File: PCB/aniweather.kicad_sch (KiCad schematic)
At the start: 26 parts, among them SW1 SW_DIP_x01, SW2 SW_Push, SW3 SW_Push, U5 TPS63001

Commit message: Final revision
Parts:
- added JP1: Jumper_2_Bridged, Resistor_THT:R_Axial_DIN0207_L6.3mm_D2.5mm_P15.24mm_Horizontal, symbol Jumper:Jumper_2_Bridged
- added R5, R6, R7: 10k, Resistor_THT:R_Axial_DIN0207_L6.3mm_D2.5mm_P10.16mm_Horizontal, symbol Device:R
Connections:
- net +3.3V: now also R5.2, R6.2, R7.2
- net CS_LCD: now also R6.1
- net GND: now also JP1.1 (A), JP1.2 (B)
- net MISO: now also R7.1
- net SD_CS: now also R5.1
- no-connect marks 3 -> 7
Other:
- moved on the sheet: C1, C2, C4, C9, R1, U1

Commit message: PCB revision
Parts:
- removed JP1: Jumper_2_Bridged, Resistor_THT:R_Axial_DIN0207_L6.3mm_D2.5mm_P15.24mm_Horizontal, symbol Jumper:Jumper_2_Bridged
- added JP1: Jumper_2_Open, Jumper:SolderJumper-2_P1.3mm_Open_Pad1.0x1.5mm, symbol Jumper:Jumper_2_Open
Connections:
- net at C6.1, R2.2, SW1.2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: now also JP1.1 (A)
- net at SW1.1, U3.2 (OUT+): now also JP1.2 (B)
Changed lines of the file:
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@@
 		(title "Aniweather")
 		(date "2024-12-05")
-		(rev "v1.5")
+		(rev "v1.6")
 		(company "Cyao")
 		(comment 1 "Anime weather station")
@@
 	)
 	(junction
+		(at 201.93 30.48)
+		(diameter 0)
+		(color 0 0 0 0)
+	)
+	(junction
 		(at 49.53 106.68)
 		(diameter 0)
@@
 	(wire
 		(pts
+			(xy 193.04 30.48) (xy 201.93 30.48)
+		)
+		(stroke
+			(width 0)
+			(type default)
+		)
+	)
+	(wire
+		(pts
 			(xy 201.93 55.88) (xy 201.93 54.61)
 		)
@@
 	(wire
 		(pts
+			(xy 193.04 33.02) (xy 193.04 30.48)
+		)
+		(stroke
+			(width 0)
+			(type default)
+		)
+	)
+	(wire
+		(pts
 			(xy 48.26 58.42) (xy 48.26 60.96)
 		)
@@
 	(wire
 		(pts
+			(xy 193.04 46.99) (xy 201.93 46.99)
+		)
+		(stroke
+			(width 0)
+			(type default)
+		)
+	)
+	(wire
+		(pts
 			(xy 36.83 106.68) (xy 31.75 106.68)
 		)
@@
 	(wire
 		(pts
+			(xy 193.04 43.18) (xy 193.04 46.99)
+		)
+		(stroke
+			(width 0)
+			(type default)
+		)
+	)
+	(wire
+		(pts
 			(xy 219.71 67.31) (xy 219.71 66.04)
 		)
@@
 	)
 	(symbol
+		(lib_id "Jumper:Jumper_2_Open")
+		(at 193.04 38.1 90)
+		(unit 1)
+		(exclude_from_sim yes)
+		(in_bom yes)
+		(on_board yes)
+		(dnp no)
+		(property "Reference" "JP1"
+			(at 173.736 36.322 90)
+			(effects
+				(font
+					(size 1.27 1.27)
+				)
+				(justify right)
+			)
+		)
+		(property "Value" "Jumper_2_Open"
+			(at 173.736 38.862 90)
+			(effects
+				(font
+					(size 1.27 1.27)
+				)
+				(justify right)
+			)
+		)
+		(property "Footprint" "Jumper:SolderJumper-2_P1.3mm_Open_Pad1.0x1.5mm"
+			(at 193.04 38.1 0)
+			(effects
+				(font
+					(size 1.27 1.27)
+				)
+				(hide yes)
+			)
+		)
+		(property "Datasheet" "~"
+			(at 193.04 38.1 0)
+			(effects
+				(font
+					(size 1.27 1.27)
+				)
+				(hide yes)
+			)
+		)
+		(property "Description" "Jumper, 2-pole, open"
+			(at 193.04 38.1 0)
+			(effects
+				(font
+					(size 1.27 1.27)
+				)
+				(hide yes)
+			)
+		)
+		(pin "1"
+		)
+		(pin "2"
+		)
+		(instances
+			(project ""
+				(path "/e7e4d5de-a607-486c-961b-1d24c88fafef"
+					(reference "JP1")
+					(unit 1)
+				)
+			)
+		)
+	)
+	(symbol
 		(lib_id "power:+3.3V")
 		(at 22.86 39.37 90)
@@
 	)
 	(symbol
-		(lib_id "power:GND")
-		(at 66.04 59.69 270)
-		(unit 1)
-		(exclude_from_sim no)
-		(in_bom yes)
-		(on_board yes)
-		(dnp no)
-		(fields_autoplaced yes)
-		(property "Reference" "#PWR023"
-			(at 59.69 59.69 0)
-			(effects
-				(font
-					(size 1.27 1.27)
-				)
-				(hide yes)
-			)
-		)
-		(property "Value" "GND"
-			(at 62.23 59.6899 90)
-			(effects
-				(font
-					(size 1.27 1.27)
-				)
-				(justify right)
-			)
-		)
-		(property "Footprint" ""
-			(at 66.04 59.69 0)
-			(effects
-				(font
-					(size 1.27 1.27)
-				)
-				(hide yes)
-			)
-		)
-		(property "Datasheet" ""
-			(at 66.04 59.69 0)
-			(effects
-				(font
-					(size 1.27 1.27)
-				)
-				(hide yes)
-			)
-		)
-		(property "Description" "Power symbol creates a global label with name \"GND\" , ground"
-			(at 66.04 59.69 0)
-			(effects
-				(font
-					(size 1.27 1.27)
-				)
-				(hide yes)
-			)
-		)
-		(pin "1"
-		)
-		(instances
-			(project "aniweather"
-				(path "/e7e4d5de-a607-486c-961b-1d24c88fafef"
-					(reference "#PWR023")
-					(unit 1)
-				)
-			)
-		)
-	)
-	(symbol
 		(lib_id "power:PWR_FLAG")
 		(at 31.75 91.44 0)
@@
 	)
 	(symbol
-		(lib_id "Jumper:Jumper_2_Bridged")
-		(at 71.12 59.69 0)
-		(unit 1)
-		(exclude_from_sim yes)
-		(in_bom yes)
-		(on_board yes)
-		(dnp no)
-		(fields_autoplaced yes)
-		(property "Reference" "JP1"
-			(at 71.12 54.61 0)
-			(effects
-				(font
-					(size 1.27 1.27)
-				)
-			)
-		)
-		(property "Value" "Jumper_2_Bridged"
-			(at 71.12 57.15 0)
-			(effects
-				(font
-					(size 1.27 1.27)
-				)
-			)
-		)
-		(property "Footprint" "Resistor_THT:R_Axial_DIN0207_L6.3mm_D2.5mm_P15.24mm_Horizontal"
-			(at 71.12 59.69 0)
-			(effects
-				(font
-					(size 1.27 1.27)
-				)
-				(hide yes)
-			)
-		)
-		(property "Datasheet" "~"
-			(at 71.12 59.69 0)
-			(effects
-				(font
-					(size 1.27 1.27)
-				)
-				(hide yes)
-			)
-		)
-		(property "Description" "Jumper, 2-pole, closed/bridged"
-			(at 71.12 59.69 0)
-			(effects
-				(font
-					(size 1.27 1.27)
-				)
-				(hide yes)
-			)
-		)
-		(pin "1"
-		)
-		(pin "2"
-		)
-		(instances
-			(project ""
-				(path "/e7e4d5de-a607-486c-961b-1d24c88fafef"
-					(reference "JP1")
-					(unit 1)
-				)
-			)
-		)
-	)
-	(symbol
 		(lib_id "power:+3.3V")
 		(at 106.68 36.83 0)
@@
 					(unit 1)
 				)
-			)
-		)
-	)
-	(symbol
-		(lib_id "power:GND")
-		(at 76.2 59.69 90)
-		(unit 1)
-		(exclude_from_sim no)
-		(in_bom yes)
-		(on_board yes)
-		(dnp no)
-		(fields_autoplaced yes)
-		(property "Reference" "#PWR022"
-			(at 82.55 59.69 0)
-			(effects
-				(font
-					(size 1.27 1.27)
-				)
-				(hide yes)
-			)
-		)
-		(property "Value" "GND"
-			(at 80.01 59.6899 90)
-			(effects
-				(font
-					(size 1.27 1.27)
-				)
-				(justify right)
-			)
-		)
-		(property "Footprint" ""
-			(at 76.2 59.69 0)
-			(effects
-				(font
-					(size 1.27 1.27)
-				)
-				(hide yes)
-			)
-		)
-		(property "Datasheet" ""
-			(at 76.2 59.69 0)
-			(effects
-				(font
-					(size 1.27 1.27)
-				)
-				(hide yes)
-			)
-		)
-		(property "Description" "Power symbol creates a global label with name \"GND\" , ground"
-			(at 76.2 59.69 0)
-			(effects
-				(font
-					(size 1.27 1.27)
-				)
-				(hide yes)
-			)
-		)
-		(pin "1"
-		)
-		(instances
-			(project "aniweather"
-				(path "/e7e4d5de-a607-486c-961b-1d24c88fafef"
-					(reference "#PWR022")
-					(unit 1)
-				)

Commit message: I hope this is the final revision
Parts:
- added JP2, JP3, JP4: Jumper_2_Open, Jumper:SolderJumper-2_P1.3mm_Open_Pad1.0x1.5mm, symbol Jumper:Jumper_2_Open
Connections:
- net GND: now also JP3.1 (A)
- net at JP1.2 (B), SW1.1, U3.2 (OUT+): now also JP4.2 (B)
- net at U3.4 (IN+): now also JP2.1 (A)
- net at U3.5 (IN-): now also JP3.2 (B)
- net VBUS: now reaches U2.14 (VBUS)
- net VBUS: now also JP2.2 (B), JP4.1 (A)
- no-connect marks 7 -> 4

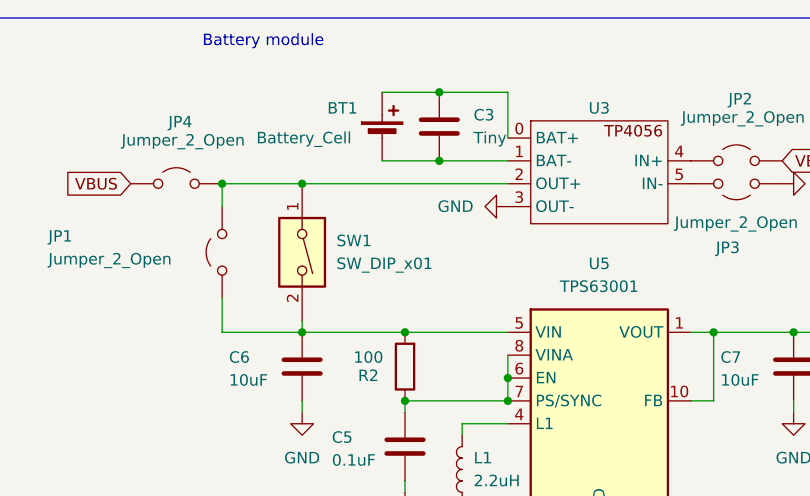
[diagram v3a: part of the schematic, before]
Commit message: Add diode
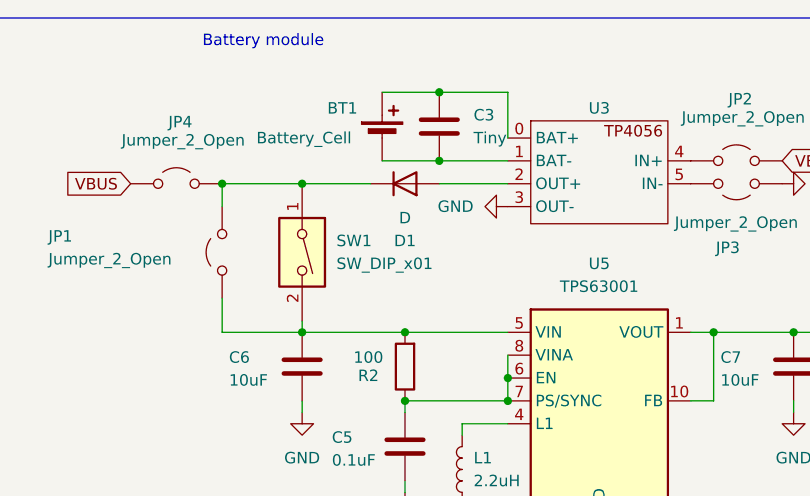
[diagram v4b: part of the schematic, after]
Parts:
- added D1: D, Diode_THT:D_DO-35_SOD27_P7.62mm_Horizontal, symbol Device:D
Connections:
- net at JP1.2 (B), JP4.2 (B), SW1.1: now also D1.1 (K); no longer U3.2 (OUT+)
- new net: D1.2 (A), U3.2 (OUT+)
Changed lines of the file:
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@@
 		(title "Aniweather")
 		(date "2024-12-05")
-		(rev "v1.7")
+		(rev "v1.8")
 		(company "Cyao")
 		(comment 1 "Anime weather station")
@@
 	)
 	(junction
+		(at 49.53 106.68)
+		(diameter 0)
+		(color 0 0 0 0)
+	)
+	(junction
+		(at 48.26 58.42)
+		(diameter 0)
+		(color 0 0 0 0)
+	)
+	(junction
+		(at 106.68 46.99)
+		(diameter 0)
+		(color 0 0 0 0)
+	)
+	(junction
+		(at 49.53 95.25)
+		(diameter 0)
+		(color 0 0 0 0)
+	)
+	(junction
+		(at 256.54 46.99)
+		(diameter 0)
+		(color 0 0 0 0)
+	)
+	(junction
+		(at 267.97 46.99)
+		(diameter 0)
+		(color 0 0 0 0)
+	)
+	(junction
 		(at 201.93 30.48)
-		(diameter 0)
-		(color 0 0 0 0)
-	)
-	(junction
-		(at 49.53 106.68)
-		(diameter 0)
-		(color 0 0 0 0)
-	)
-	(junction
-		(at 48.26 58.42)
-		(diameter 0)
-		(color 0 0 0 0)
-	)
-	(junction
-		(at 106.68 46.99)
-		(diameter 0)
-		(color 0 0 0 0)
-	)
-	(junction
-		(at 49.53 95.25)
-		(diameter 0)
-		(color 0 0 0 0)
-	)
-	(junction
-		(at 256.54 46.99)
-		(diameter 0)
-		(color 0 0 0 0)
-	)
-	(junction
-		(at 267.97 46.99)
 		(diameter 0)
 		(color 0 0 0 0)
@@
 	(wire
 		(pts
-			(xy 201.93 30.48) (xy 224.79 30.48)
-		)
-		(stroke
-			(width 0)
-			(type default)
-		)
-	)
-	(wire
-		(pts
 			(xy 49.53 91.44) (xy 49.53 95.25)
 		)
@@
 	(wire
 		(pts
+			(xy 217.17 30.48) (xy 224.79 30.48)
+		)
+		(stroke
+			(width 0)
+			(type default)
+		)
+	)
+	(wire
+		(pts
 			(xy 269.24 46.99) (xy 267.97 46.99)
 		)
@@
 		(pts
 			(xy 213.36 46.99) (xy 224.79 46.99)
+		)
+		(stroke
+			(width 0)
+			(type default)
+		)
+	)
+	(wire
+		(pts
+			(xy 201.93 30.48) (xy 209.55 30.48)
 		)
 		(stroke
@@
 					(unit 1)
 				)
+			)
+		)
+	)
+	(symbol
+		(lib_id "Device:D")
+		(at 213.36 30.48 0)
+		(mirror x)
+		(unit 1)
+		(exclude_from_sim no)
+		(in_bom yes)
+		(on_board yes)
+		(dnp no)
+		(property "Reference" "D1"
+			(at 213.36 36.83 0)
+			(effects
+				(font
+					(size 1.27 1.27)
+				)
+			)
+		)
+		(property "Value" "D"
+			(at 213.36 34.29 0)
+			(effects
+				(font
+					(size 1.27 1.27)
+				)
+			)
+		)
+		(property "Footprint" "Diode_THT:D_DO-35_SOD27_P7.62mm_Horizontal"
+			(at 213.36 30.48 0)
+			(effects
+				(font
+					(size 1.27 1.27)
+				)
+				(hide yes)
+			)
+		)
+		(property "Datasheet" "~"
+			(at 213.36 30.48 0)
+			(effects
+				(font
+					(size 1.27 1.27)
+				)
+				(hide yes)
+			)
+		)
+		(property "Description" "Diode"
+			(at 213.36 30.48 0)
+			(effects
+				(font
+					(size 1.27 1.27)
+				)
+				(hide yes)
+			)
+		)
+		(property "Sim.Device" "D"
+			(at 213.36 30.48 0)
+			(effects
+				(font
+					(size 1.27 1.27)
+				)
+				(hide yes)
+			)
+		)
+		(property "Sim.Pins" "1=K 2=A"
+			(at 213.36 30.48 0)
+			(effects
+				(font
+					(size 1.27 1.27)
+				)
+				(hide yes)
+			)
+		)
+		(pin "1"
+		)
+		(pin "2"
+		)
+		(instances
+			(project ""
+				(path "/e7e4d5de-a607-486c-961b-1d24c88fafef"
+					(reference "D1")
+					(unit 1)
+				)

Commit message: Hope last rev
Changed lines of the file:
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@@
 	(rectangle
 		(start 165.1 12.065)
-		(end 285.115 79.375)
+		(end 285.115 79.248)
 		(stroke
 			(width 0)
@@
 	)
 	(rectangle
-		(start 94.615 12.065)
+		(start 94.488 12.065)
 		(end 165.1 79.248)
 		(stroke

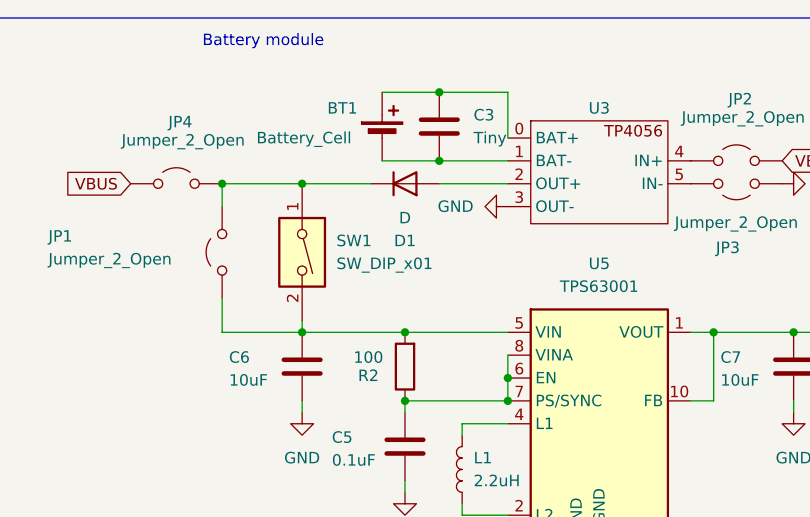
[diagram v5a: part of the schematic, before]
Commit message: Add diode to increase current capacity
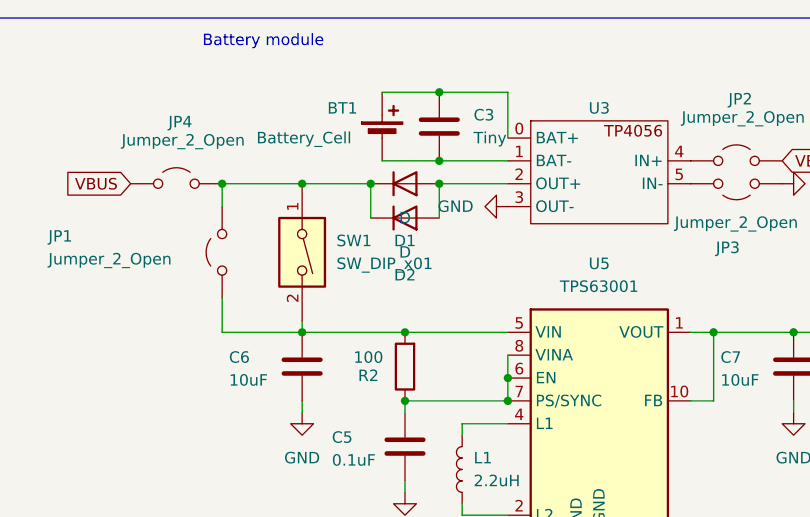
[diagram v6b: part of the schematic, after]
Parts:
- added D2: D, Diode_THT:D_DO-35_SOD27_P7.62mm_Horizontal, symbol Device:D
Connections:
- net at D1.1 (K), JP1.2 (B), JP4.2 (B)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: now also D2.1 (K)
- net at D1.2 (A), U3.2 (OUT+): now also D2.2 (A)
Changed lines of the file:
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@@
 		(title "Aniweather")
 		(date "2024-12-05")
-		(rev "v1.8")
+		(rev "v1.9")
 		(company "Cyao")
 		(comment 1 "Anime weather station")
@@
 	)
 	(junction
+		(at 217.17 30.48)
+		(diameter 0)
+		(color 0 0 0 0)
+	)
+	(junction
 		(at 31.75 129.54)
+		(diameter 0)
+		(color 0 0 0 0)
+	)
+	(junction
+		(at 209.55 30.48)
 		(diameter 0)
 		(color 0 0 0 0)
@@
 	(wire
 		(pts
+			(xy 209.55 30.48) (xy 209.55 34.29)
+		)
+		(stroke
+			(width 0)
+			(type default)
+		)
+	)
+	(wire
+		(pts
 			(xy 217.17 30.48) (xy 224.79 30.48)
 		)
@@
 		(pts
 			(xy 35.56 58.42) (xy 38.1 58.42)
+		)
+		(stroke
+			(width 0)
+			(type default)
+		)
+	)
+	(wire
+		(pts
+			(xy 217.17 30.48) (xy 217.17 34.29)
 		)
 		(stroke
@@
 					(unit 1)
 				)
+			)
+		)
+	)
+	(symbol
+		(lib_id "Device:D")
+		(at 213.36 34.29 0)
+		(mirror x)
+		(unit 1)
+		(exclude_from_sim no)
+		(in_bom yes)
+		(on_board yes)
+		(dnp no)
+		(property "Reference" "D2"
+			(at 213.36 40.64 0)
+			(effects
+				(font
+					(size 1.27 1.27)
+				)
+			)
+		)
+		(property "Value" "D"
+			(at 213.36 38.1 0)
+			(effects
+				(font
+					(size 1.27 1.27)
+				)
+			)
+		)
+		(property "Footprint" "Diode_THT:D_DO-35_SOD27_P7.62mm_Horizontal"
+			(at 213.36 34.29 0)
+			(effects
+				(font
+					(size 1.27 1.27)
+				)
+				(hide yes)
+			)
+		)
+		(property "Datasheet" "~"
+			(at 213.36 34.29 0)
+			(effects
+				(font
+					(size 1.27 1.27)
+				)
+				(hide yes)
+			)
+		)
+		(property "Description" "Diode"
+			(at 213.36 34.29 0)
+			(effects
+				(font
+					(size 1.27 1.27)
+				)
+				(hide yes)
+			)
+		)
+		(property "Sim.Device" "D"
+			(at 213.36 34.29 0)
+			(effects
+				(font
+					(size 1.27 1.27)
+				)
+				(hide yes)
+			)
+		)
+		(property "Sim.Pins" "1=K 2=A"
+			(at 213.36 34.29 0)
+			(effects
+				(font
+					(size 1.27 1.27)
+				)
+				(hide yes)
+			)
+		)
+		(pin "1"
+		)
+		(pin "2"
+		)
+		(instances
+			(project "aniweather"
+				(path "/e7e4d5de-a607-486c-961b-1d24c88fafef"
+					(reference "D2")
+					(unit 1)
+				)

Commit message: Readme and last rev
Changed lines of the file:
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@@
 		(title "Aniweather")
 		(date "2024-12-05")
-		(rev "v1.9")
+		(rev "v1.10")
 		(company "Cyao")
 		(comment 1 "Anime weather station")
@@
 	(text "Battery module"
 		(exclude_from_sim no)
-		(at 197.612 14.732 0)
+		(at 221.234 15.24 0)
 		(effects
 			(font
@@
 		(dnp no)
 		(property "Reference" "D2"
-			(at 213.36 40.64 0)
+			(at 216.154 35.814 0)
 			(effects
 				(font
@@
 		)
 		(property "Value" "D"
-			(at 213.36 38.1 0)
+			(at 216.154 33.274 0)
 			(effects
 				(font
@@
 		(dnp no)
 		(property "Reference" "D1"
-			(at 213.36 36.83 0)
+			(at 215.9 31.75 0)
 			(effects
 				(font
@@
 		)
 		(property "Value" "D"
-			(at 213.36 34.29 0)
-			(effects
-				(font
+			(at 215.9 29.21 0)
+			(effects
+				(font

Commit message: Improve inductor footprint
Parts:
- L1: footprint Inductor_SMD:L_1210_3225Metric -> asylum:NR3015T2R2M
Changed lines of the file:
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@@
 (kicad_sch
-	(version 20241004)
+	(version 20250114)
 	(generator "eeschema")
-	(generator_version "8.99")
+	(generator_version "9.0")
 	(paper "A4")
 	(title_block
@@
 			)
 		)
-		(property "Footprint" "Inductor_SMD:L_1210_3225Metric"
+		(property "Footprint" "asylum:NR3015T2R2M"
 			(at 219.71 62.23 0)
 			(effects
